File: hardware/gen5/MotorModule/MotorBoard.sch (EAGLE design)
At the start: 46 parts, among them IC2 3.3V REG, J1 M20X2SHROUDED

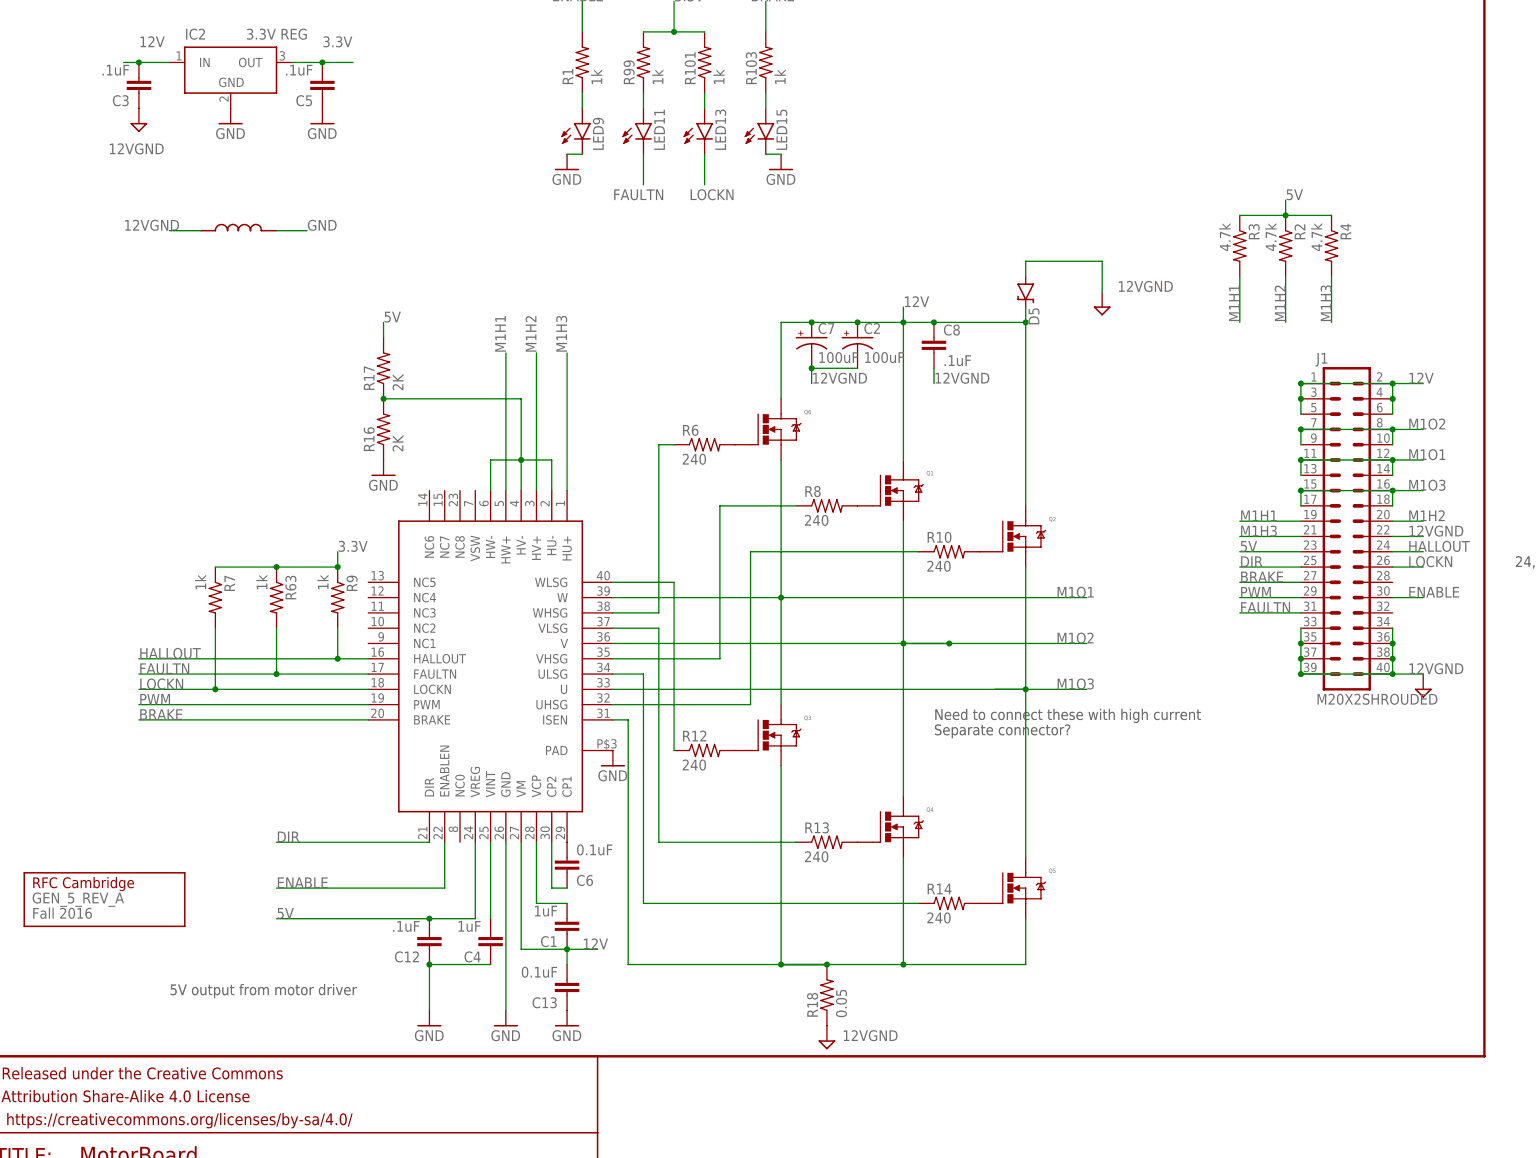
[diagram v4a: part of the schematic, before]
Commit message: few minor motor board fixes
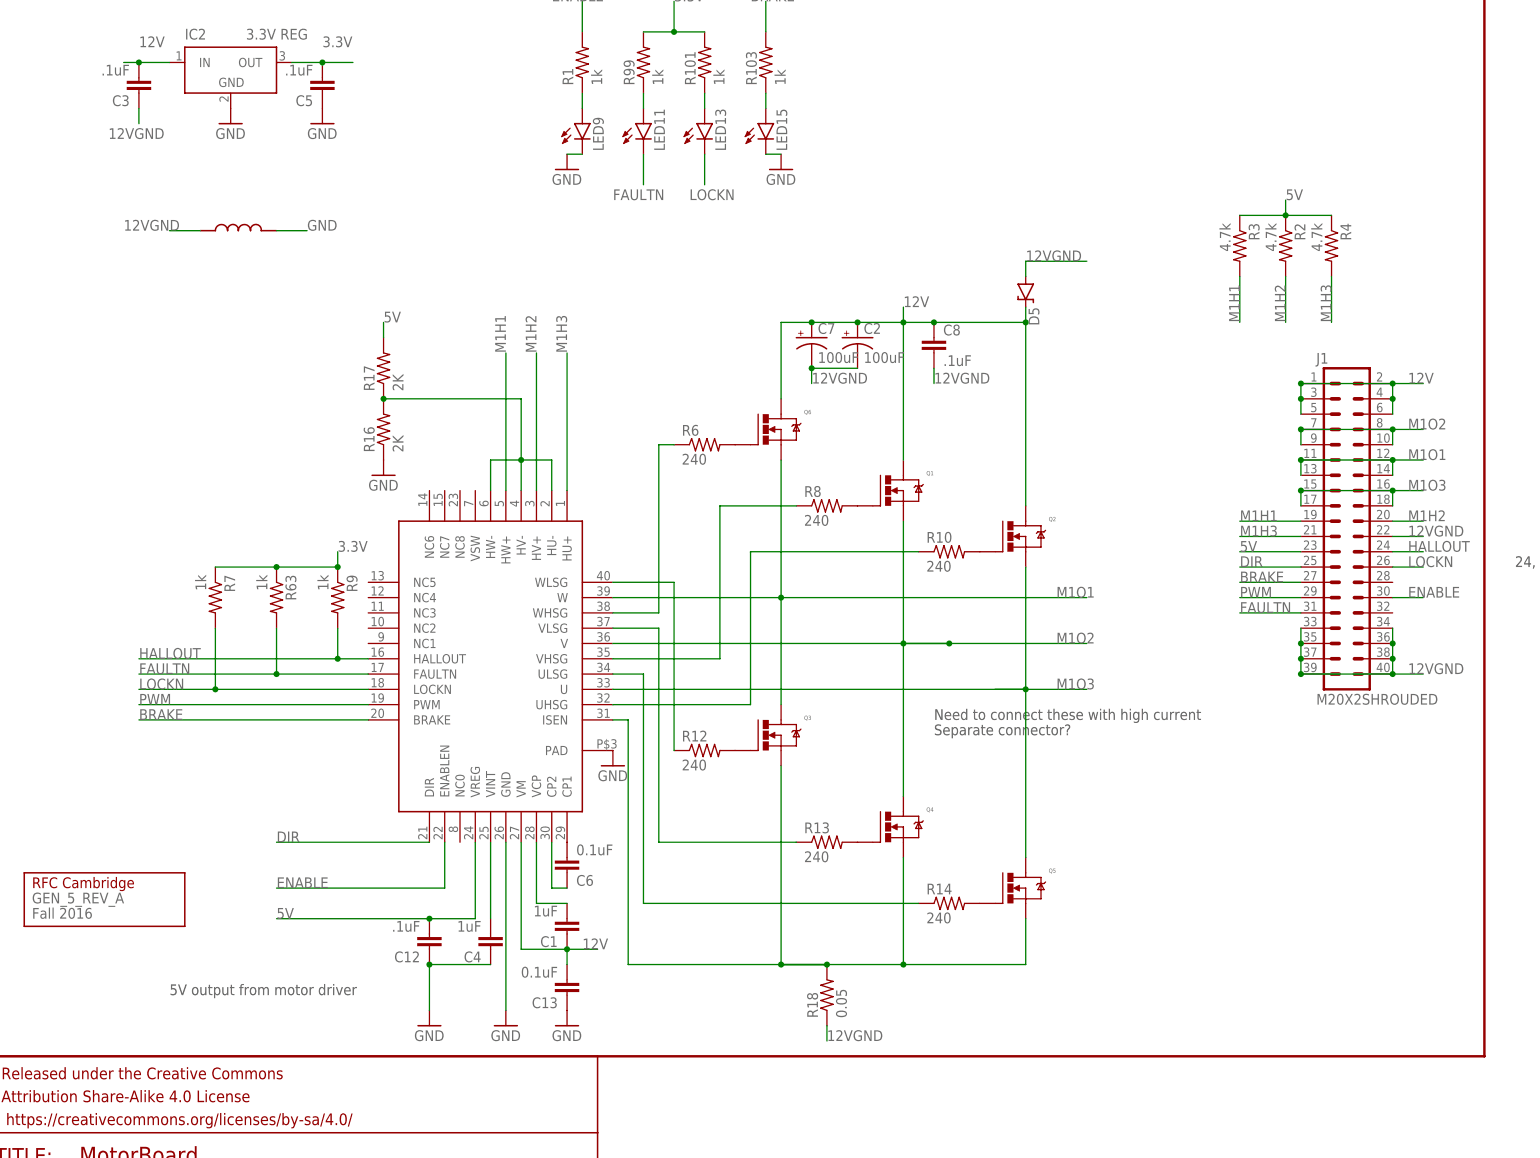
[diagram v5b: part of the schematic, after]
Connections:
- net 12VGND: now also C3.1
- net GND: no longer C3.1
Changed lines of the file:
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@@
 <part name="R18" library="resistor" deviceset="R-US_" device="R2512" value="0.05"/>
 <part name="U$2" library="gen3" deviceset="INDUCTOR" device=""/>
-<part name="12VGND" library="supply2" deviceset="GND" device=""/>
-<part name="12VGND1" library="supply2" deviceset="GND" device=""/>
-<part name="12VGND2" library="supply2" deviceset="GND" device=""/>
 <part name="R2" library="SparkFun-Resistors" deviceset="RESISTOR" device="0805-RES" value="4.7k"/>
 <part name="R3" library="SparkFun-Resistors" deviceset="RESISTOR" device="0805-RES" value="4.7k"/>
@@
 <part name="GND1" library="SparkFun-Aesthetics" deviceset="GND" device=""/>
 <part name="J1" library="SparkFun-Connectors" deviceset="M20X2" device="SHROUDED"/>
-<part name="12VGND4" library="supply2" deviceset="GND" device=""/>
 </parts>
 <sheets>
@@
 <instance part="R18" gate="G$1" x="139.7" y="10.16" rot="R90"/>
 <instance part="U$2" gate="G$1" x="35.56" y="137.16"/>
-<instance part="12VGND" gate="GND" x="25.4" y="154.94"/>
-<instance part="12VGND1" gate="GND" x="185.42" y="124.46"/>
-<instance part="12VGND2" gate="GND" x="139.7" y="2.54"/>
 <instance part="R2" gate="G$1" x="215.9" y="134.62" rot="R270"/>
 <instance part="R3" gate="G$1" x="208.28" y="134.62" rot="R270"/>
@@
 <instance part="GND1" gate="1" x="132.08" y="147.32"/>
 <instance part="J1" gate="G$1" x="226.06" y="88.9"/>
-<instance part="12VGND4" gate="GND" x="238.76" y="60.96"/>
 </instances>
 <busses>
@@
 <wire x1="48.26" y1="137.16" x2="53.34" y2="137.16" width="0.1524" layer="91"/>
 <label x="53.34" y="137.16" size="1.778" layer="95"/>
-</segment>
-<segment>
-<pinref part="C3" gate="G$1" pin="1"/>
-<pinref part="12VGND" gate="GND" pin="GND"/>
 </segment>
 <segment>
@@
 </segment>
 <segment>
-<label x="187.96" y="127" size="1.778" layer="95"/>
+<label x="172.72" y="132.08" size="1.778" layer="95"/>
 <wire x1="172.72" y1="129.54" x2="172.72" y2="132.08" width="0.1524" layer="91"/>
 <pinref part="D5" gate="G$1" pin="A"/>
 <label x="22.86" y="137.16" size="1.778" layer="95"/>
-<wire x1="172.72" y1="132.08" x2="185.42" y2="132.08" width="0.1524" layer="91"/>
-<wire x1="185.42" y1="132.08" x2="185.42" y2="127" width="0.1524" layer="91"/>
-<label x="20.32" y="149.86" size="1.778" layer="95"/>
-<pinref part="12VGND1" gate="GND" pin="GND"/>
+<wire x1="172.72" y1="132.08" x2="182.88" y2="132.08" width="0.1524" layer="91"/>
+<label x="20.32" y="152.4" size="1.778" layer="95"/>
 </segment>
 <segment>
 <pinref part="R18" gate="G$1" pin="1"/>
-<label x="142.24" y="2.54" size="1.778" layer="95"/>
-<pinref part="12VGND2" gate="GND" pin="GND"/>
+<label x="139.7" y="2.54" size="1.778" layer="95"/>
+<wire x1="139.7" y1="2.54" x2="139.7" y2="5.08" width="0.1524" layer="91"/>
 </segment>
 <segment>
@@
 <wire x1="233.68" y1="63.5" x2="238.76" y2="63.5" width="0.1524" layer="91"/>
 <label x="236.22" y="63.5" size="1.778" layer="95"/>
-<pinref part="12VGND4" gate="GND" pin="GND"/>
 <pinref part="J1" gate="G$1" pin="33"/>
 <wire x1="218.44" y1="68.58" x2="218.44" y2="71.12" width="0.1524" layer="91"/>
@@
 <label x="236.22" y="86.36" size="1.778" layer="95"/>
 </segment>
+<segment>
+<pinref part="C3" gate="G$1" pin="1"/>
+<wire x1="25.4" y1="154.94" x2="25.4" y2="157.48" width="0.1524" layer="91"/>
+</segment>
 </net>

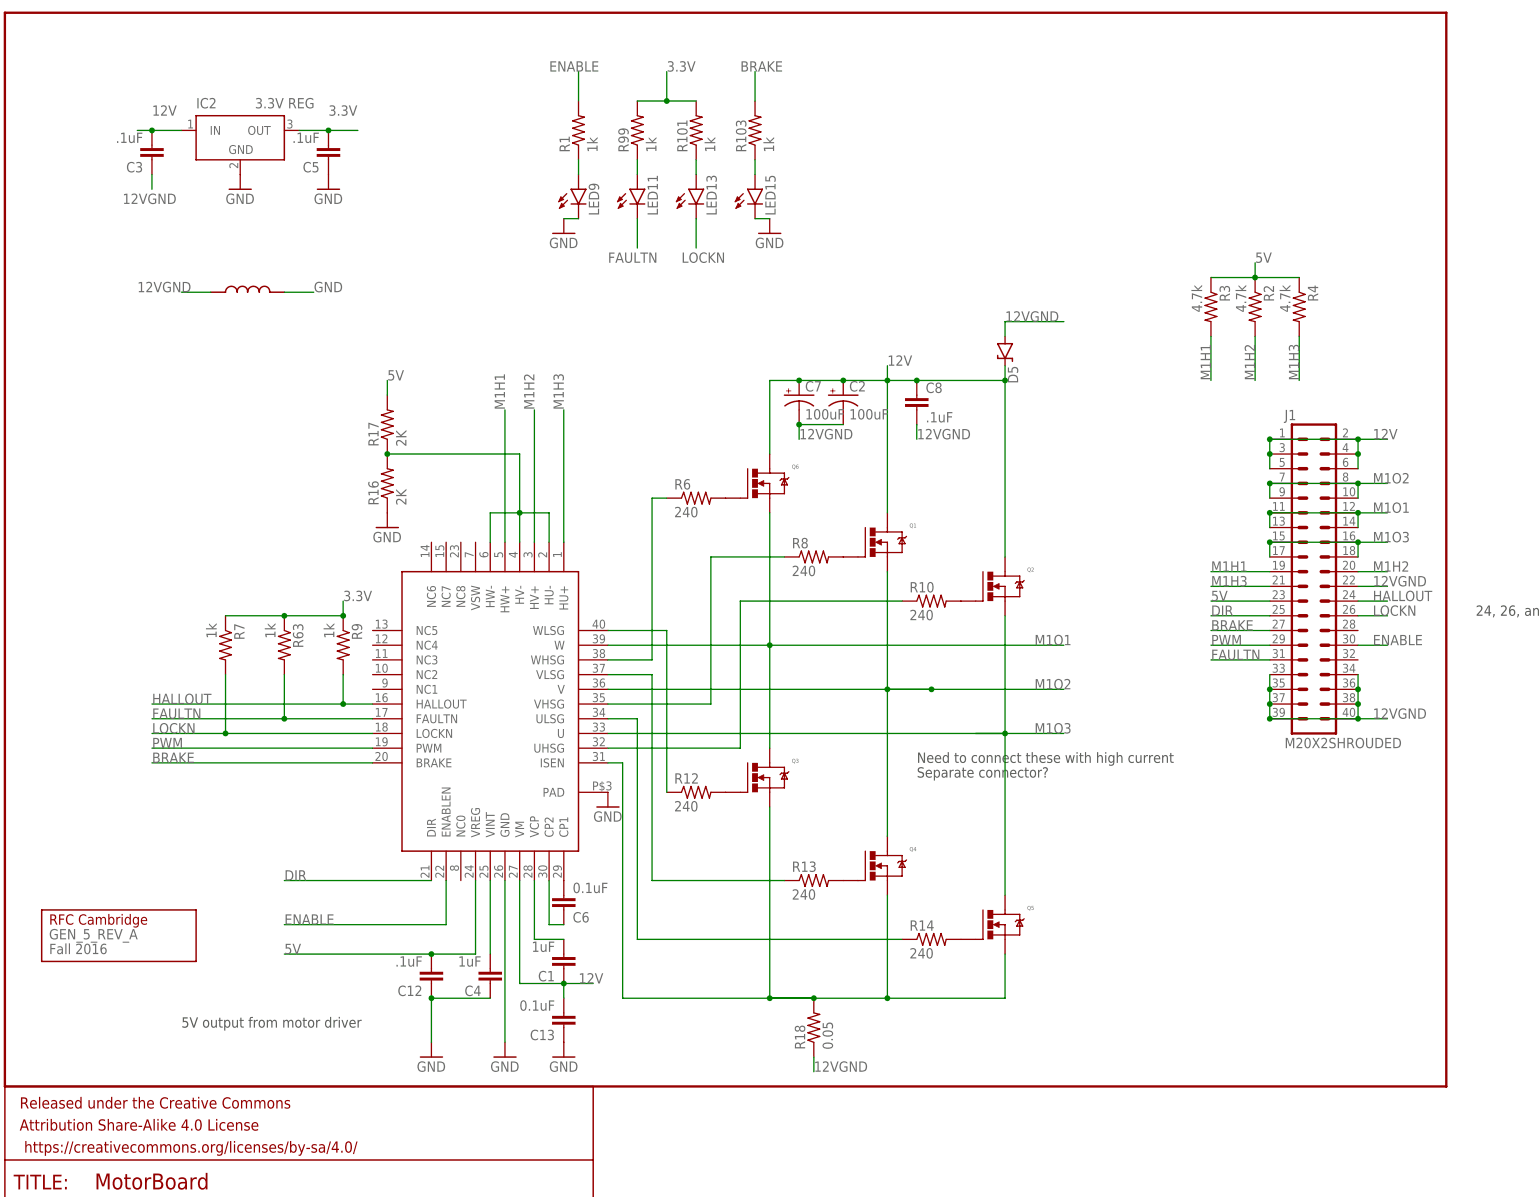
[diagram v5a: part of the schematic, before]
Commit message: updated motor board
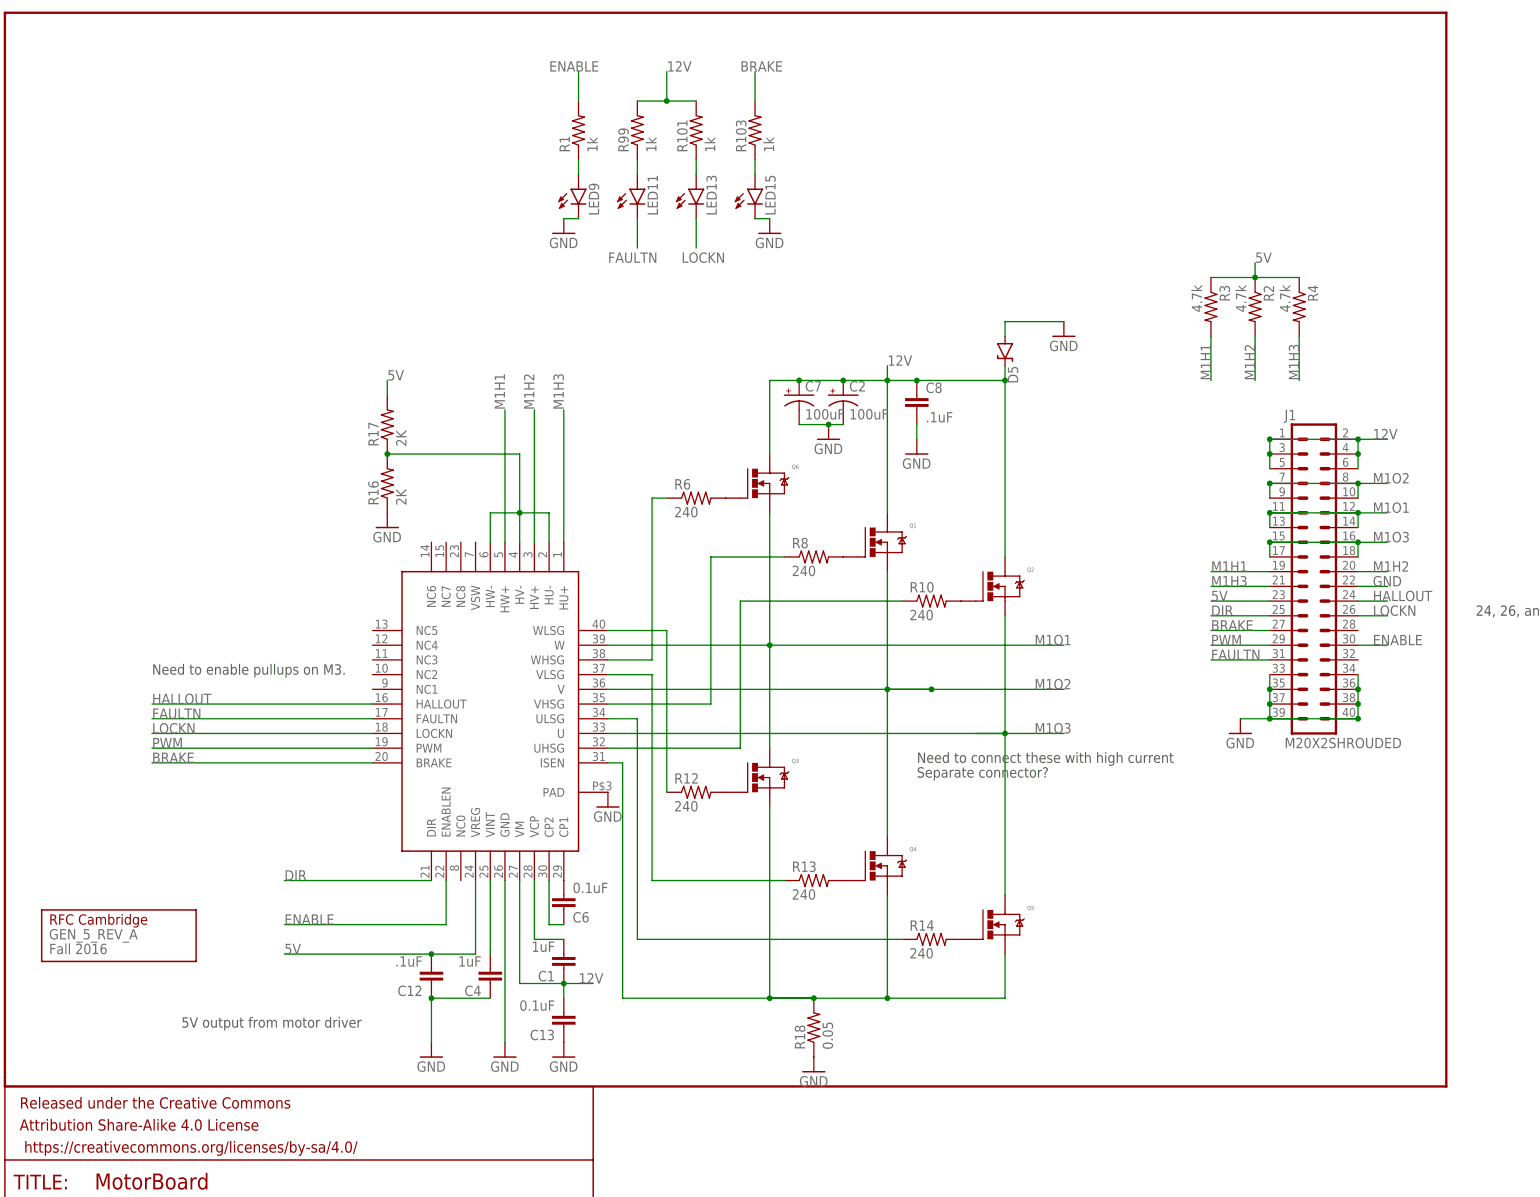
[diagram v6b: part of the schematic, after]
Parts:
- removed C3, C5: .1uF, SparkFun-Capacitors:CAP0805
- removed IC2: 3.3V REG, linear-technology:LT1129CST5
- removed R63, R7, R9: 1k, SparkFun-Resistors:RESISTOR0805-RES
- removed U$2: INDUCTOR, gen3:INDUCTOR
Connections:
- removed net 12VGND: C2.-, C3.1, C7.-, C8.2, D5.A, J1.22, J1.33, J1.34, J1.35, J1.36, J1.37, J1.38, J1.39, J1.40, R18.1, U$2.P$1
- removed net 3.3V: C5.2, IC2G$1.OUT, R101.2, R63.1, R7.1, R9.1, R99.2
- net 12V: now also R101.2, R99.2; no longer C3.2, IC2G$1.IN
- net FAULTN: no longer R63.2
- net GND: now also C2.-, C7.-, C8.2, D5.A, J1.22, J1.33, J1.34, J1.35, J1.36, J1.37, J1.38, J1.39, J1.40, R18.1; no longer C5.1, IC2G$1.GND, U$2.P$2
- net HALLOUT: no longer R9.2
- net LOCKN: no longer R7.2
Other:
- note added: "Need to enable pullups on M3."
